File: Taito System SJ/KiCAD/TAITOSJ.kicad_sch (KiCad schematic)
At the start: 0 parts

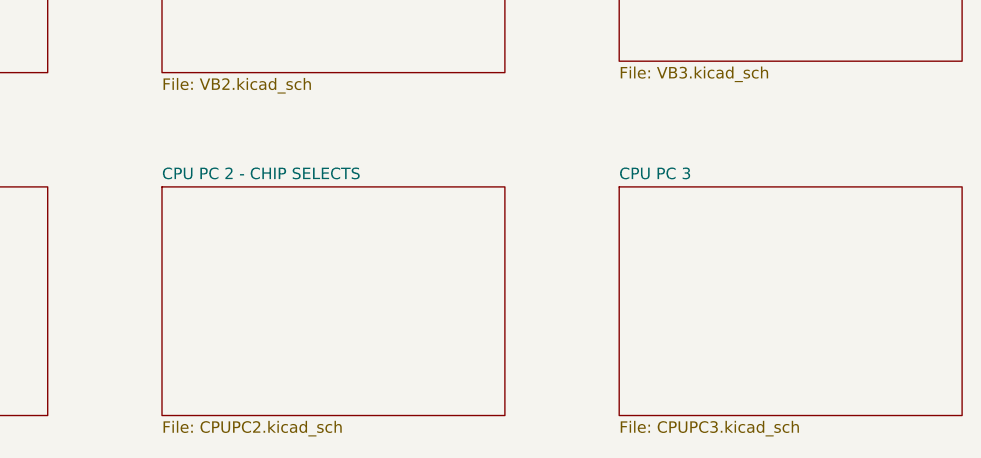
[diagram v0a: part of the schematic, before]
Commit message: Added CPU
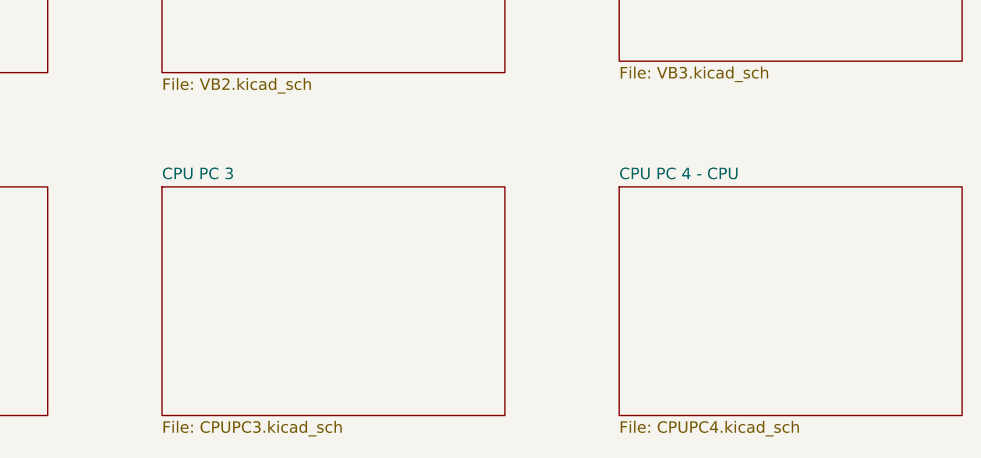
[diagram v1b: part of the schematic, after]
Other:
- removed sheet CPU PC 2 - CHIP SELECTS
- added sheet CPU PC 4 - CPU (CPUPC4.kicad_sch)

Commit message: Start of gameboard
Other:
- added sheet Sound - CPU (sound1.kicad_sch)
- added sheet Sound Chips (game2.kicad_sch)
- added sheet Sound Chips - IO (game3.kicad_sch)

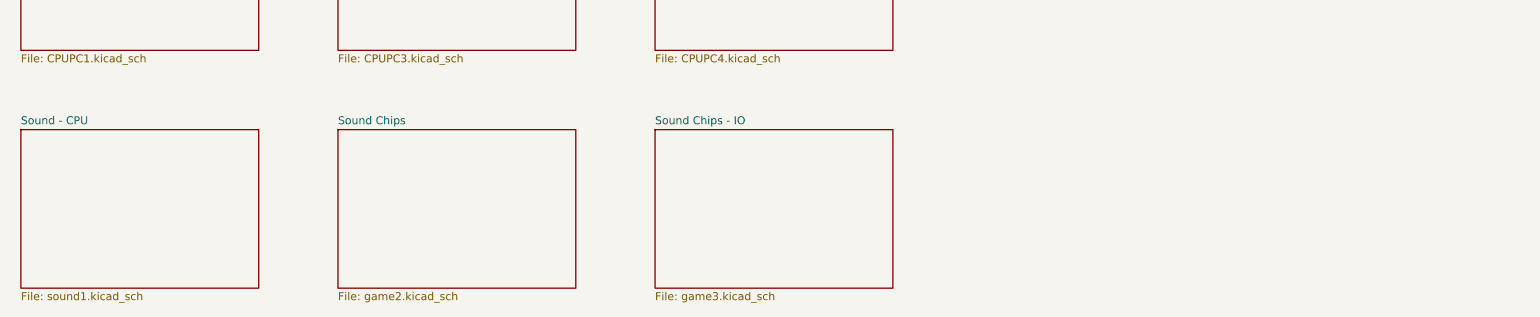
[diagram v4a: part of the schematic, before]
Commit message: RGB output & Start of Hit Bus
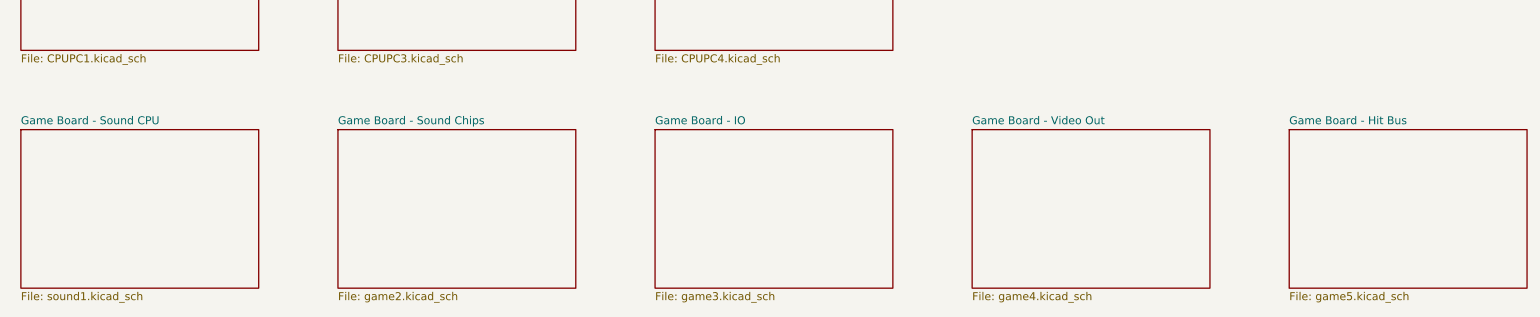
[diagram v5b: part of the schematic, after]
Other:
- sheet Sound - CPU renamed Game Board - Sound CPU
- sheet Sound Chips renamed Game Board - Sound Chips
- sheet Sound Chips - IO renamed Game Board - IO
- added sheet Game Board - Hit Bus (game5.kicad_sch)
- added sheet Game Board - Video Out (game4.kicad_sch)

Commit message: Update before transfer
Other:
- added sheet Game Board (game6.kicad_sch)

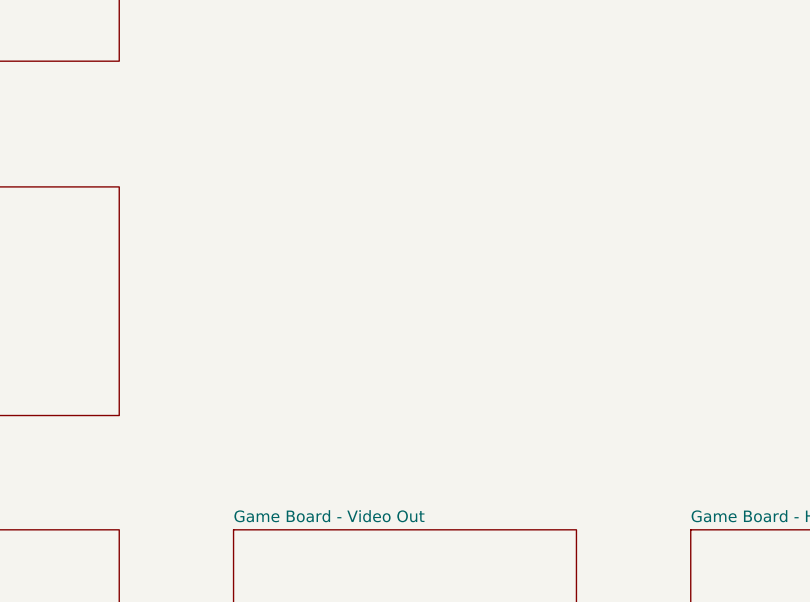
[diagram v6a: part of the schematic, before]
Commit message: Added MCU to Taito SJ Schematics
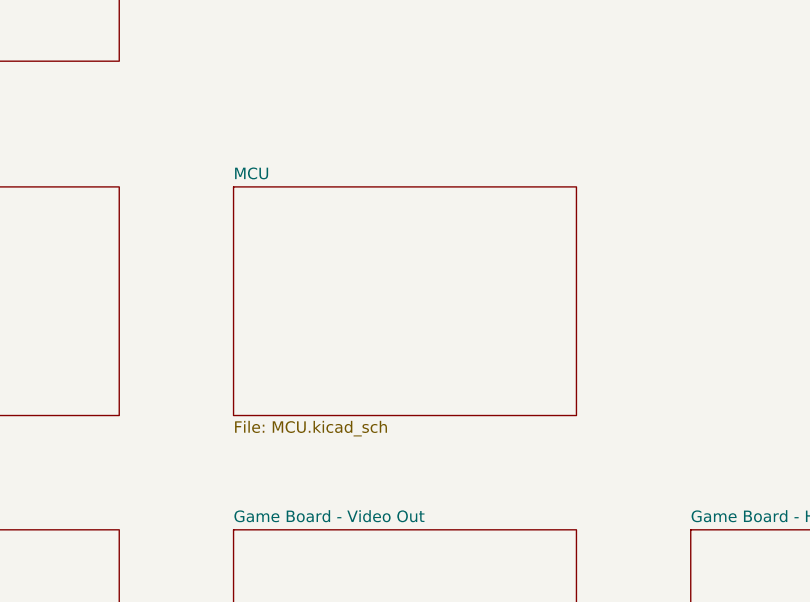
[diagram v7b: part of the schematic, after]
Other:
- added sheet MCU (MCU.kicad_sch)

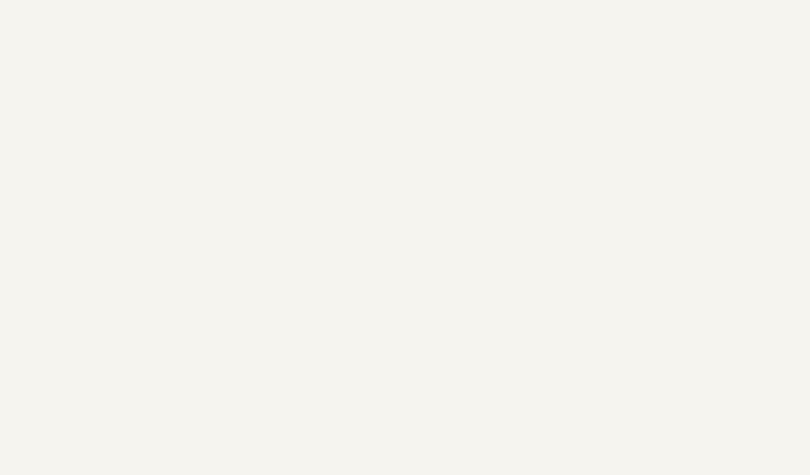
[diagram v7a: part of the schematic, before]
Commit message: Updated Taito SJ Schematics
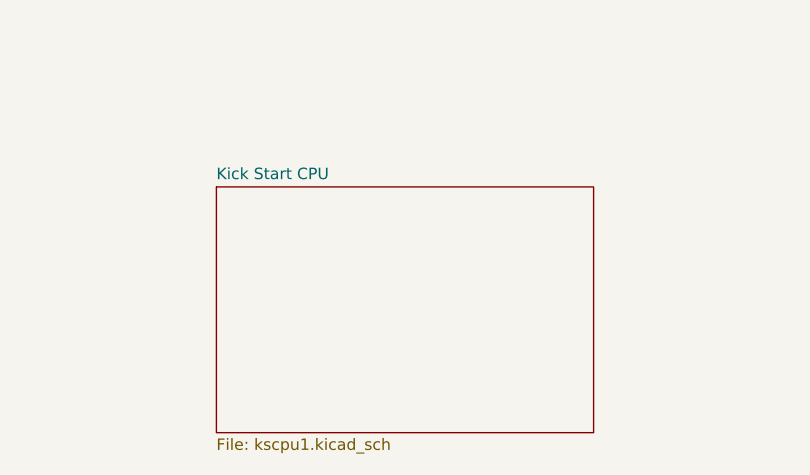
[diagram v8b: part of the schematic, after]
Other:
- added sheet Kick Start CPU (kscpu1.kicad_sch)
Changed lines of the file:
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@@
+	)
+	(sheet
+		(at 186.69 188.595)
+		(size 41.91 27.305)
+		(exclude_from_sim no)
+		(in_bom yes)
+		(on_board yes)
+		(dnp no)
+		(fields_autoplaced yes)
+		(stroke
+			(width 0.1524)
+			(type solid)
+		)
+		(fill
+			(color 0 0 0 0.0000)
+		)
+		(property "Sheetname" "Kick Start CPU"
+			(at 186.69 187.8834 0)
+			(effects
+				(font
+					(size 1.27 1.27)
+				)
+				(justify left bottom)
+			)
+		)
+		(property "Sheetfile" "kscpu1.kicad_sch"
+			(at 186.69 216.4846 0)
+			(effects
+				(font
+					(size 1.27 1.27)
+				)
+				(justify left top)
+			)
+		)
+		(instances
+			(project "TAITOSJ"
+				(path "/c9398d89-67dd-4ff5-9367-82e2b6879830"
+					(page "17")
+				)
+			)
+		)
 	)
 	(sheet
